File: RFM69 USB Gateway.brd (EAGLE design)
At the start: 42.3 x 17.1 mm, 22 parts, among them CN1 MINIB, IC3 MCP1703CB, U1 FT231XS, X1 16 MHz

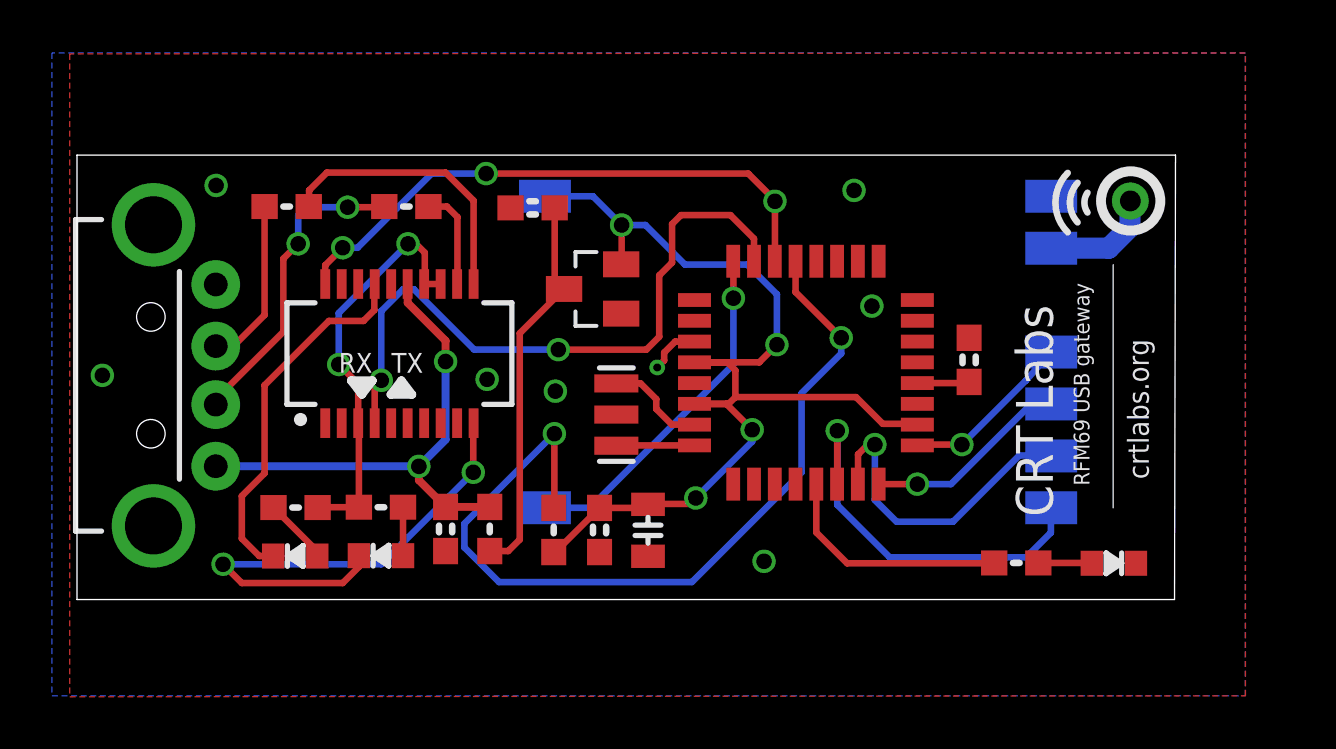
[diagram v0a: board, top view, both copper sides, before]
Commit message: Added ISP header and reset button
v0.4
- ISP header
- Reset button
- Silk screen for all components
- Slight rearrangement
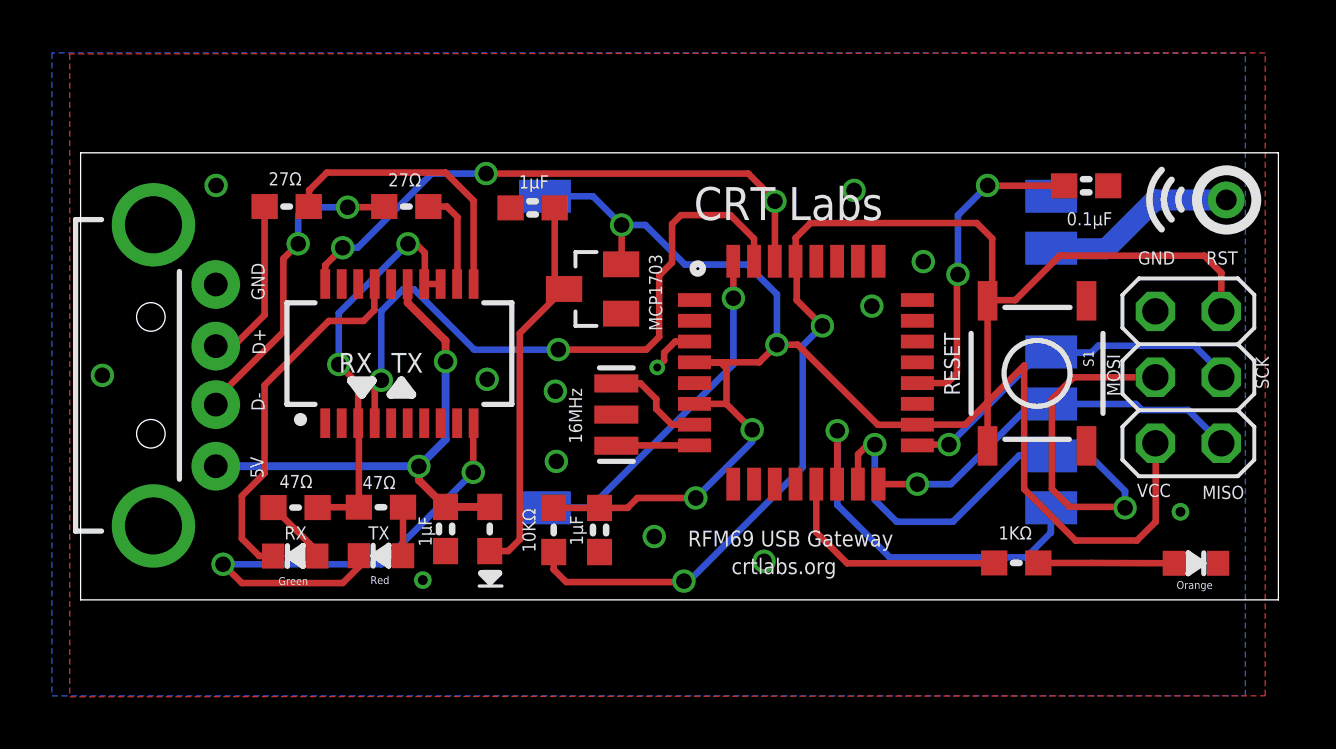
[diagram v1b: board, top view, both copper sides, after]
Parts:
- removed C3: 10u, LowPowerLab:0805-CAP
- added JP1: (no value), pinhead:2X03
- added S1: SWITCH-MOMENTARY-2SMD-ALT01, Testing:TACTILE-SWITCH-SMD-ALT01
- C4: value 0.1 -> 1u
- R2: value 1k5 -> 1k
- moved C5 8.08 mm to (50.9, 18.9), turned to 0 degrees
- moved U$1 3.70 mm to (56.3, 18.3)
- moved U$2 3.16 mm to (55.1, 4.34)
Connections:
- removed net RST: ATMEGA328.29, R1.2
- new net RESET: ATMEGA328.29, JP1.5, R1.1, S1.3, S1.4
- net D11_MOSI: now also JP1.4
- net D12_MISO: now also JP1.1
- net D13_SCK: now also JP1.3
- net GND: now also JP1.6, S1.1, S1.2; no longer C3.2
- net VCC: now also JP1.2, R1.2; no longer C3.1, R1.1
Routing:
- net RESET: track 0.00 -> 49.4 mm, vias 0 -> 2
- net RST: track 33.5 -> 0.00 mm, vias 2 -> 0
- net VCC: track 41.8 -> 57.6 mm
- net D11_MOSI: track 12.3 -> 27.3 mm, vias 1 -> 2
- net AREF: track 2.01 -> 12.4 mm, vias 0 -> 2
- net D13_SCK: track 6.68 -> 13.9 mm
- net D12_MISO: track 7.93 -> 15.1 mm
- net N$2: track 2.06 -> 5.22 mm
- net N$3: track 4.38 -> 7.53 mm
- net GND: vias 8 -> 13
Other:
- board size 42.3 x 17.1 mm -> 46.1 x 17.2 mm
- board text added: "0.1μF"
- board text added: "10KΩ"
- board text added: "16MHz"
- board text added: "1KΩ"
- board text added: "1μF"
- board text added: "27Ω"
- board text added: "47Ω"
- board text added: "5V"
- board text added: "D+"
- board text added: "D-"
- board text added: "GND"
- board text added: "Green"
- board text added: "MCP1703"
- board text added: "MISO"
- board text added: "MOSI"
- board text added: "Orange"
- board text added: "RESET"
- board text added: "RFM69 USB Gateway"
- board text added: "RST"
- board text added: "Red"
- board text added: "SCK"
- board text added: "VCC"
- board text added: "v0.4 2016"
- board text removed: "RFM69 USB gateway"
- board text removed: "v0.3 2016"

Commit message: Fixed overlapping traces
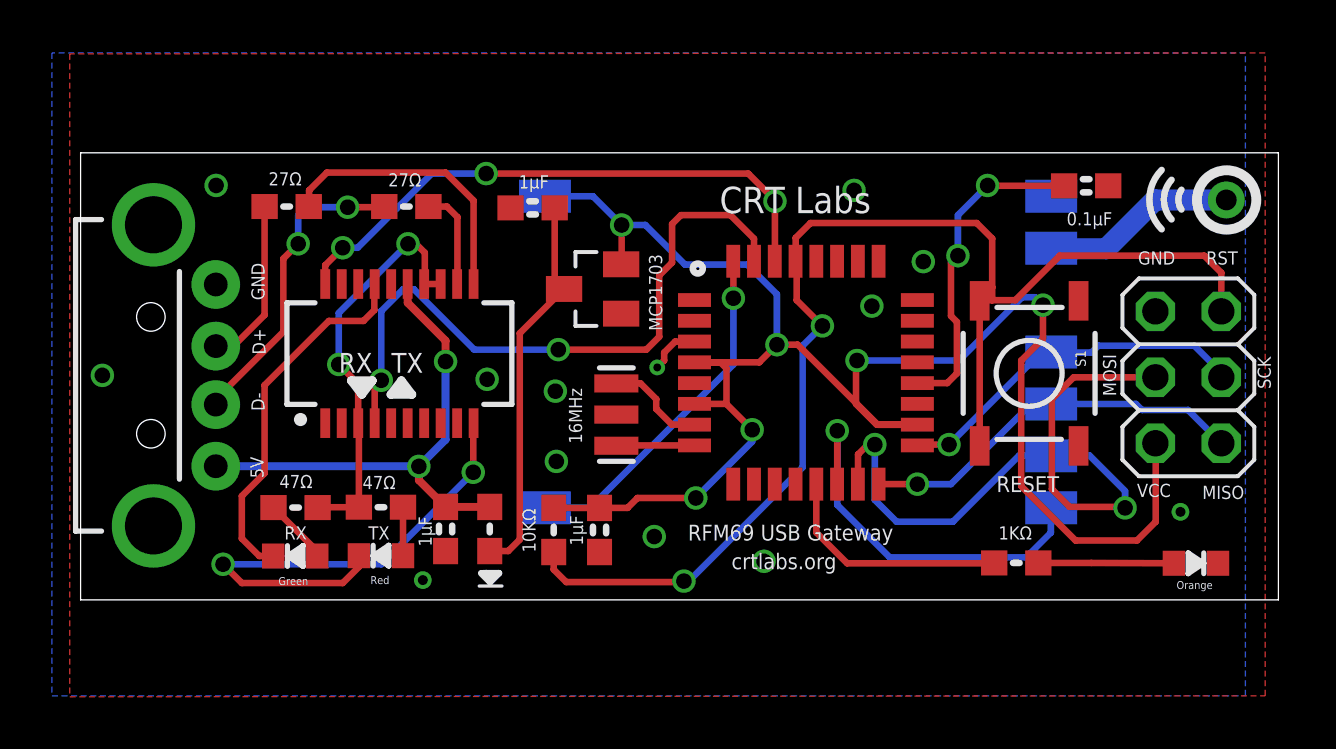
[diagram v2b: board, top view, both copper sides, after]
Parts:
- moved S1 0.30 mm to (48.7, 11.7)
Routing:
- net VCC: track 57.6 -> 68.0 mm, vias 4 -> 6
- net RESET: track 49.4 -> 49.9 mm
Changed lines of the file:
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@@
 <wire x1="27.7749" y1="3.9624" x2="27.9654" y2="3.7719" width="0.254" layer="21"/>
 <wire x1="28.3845" y1="3.4671" x2="27.5082" y2="3.4671" width="0.127" layer="21"/>
-<text x="45.4152" y="13.2207" size="0.6096" layer="121" font="vector" ratio="7" rot="R270">RESET</text>
+<text x="47.4345" y="7.0866" size="0.6096" layer="121" font="vector" ratio="7">RESET</text>
 <text x="55.5117" y="15.8496" size="0.508" layer="121" font="vector" ratio="7">RST</text>
 <text x="52.8828" y="15.8496" size="0.508" layer="121" font="vector" ratio="7">GND</text>
 <text x="52.8447" y="6.8961" size="0.508" layer="121" font="vector" ratio="7">VCC</text>
 <text x="55.3593" y="6.8199" size="0.508" layer="121" font="vector" ratio="7">MISO</text>
-<text x="52.197" y="10.7823" size="0.508" layer="121" font="vector" ratio="7" rot="R90">MOSI</text>
-<text x="57.4167" y="12.3063" size="0.508" layer="121" font="vector" ratio="7" rot="R270">SCK</text>
+<text x="52.0446" y="10.7823" size="0.508" layer="121" font="vector" ratio="7" rot="R90">MOSI</text>
+<text x="57.4929" y="12.3063" size="0.508" layer="121" font="vector" ratio="7" rot="R270">SCK</text>
 <wire x1="58.293" y1="2.9337" x2="12.1539" y2="2.9337" width="0" layer="20"/>
 <wire x1="12.1539" y1="2.9337" x2="12.1539" y2="20.1549" width="0" layer="20"/>
 <wire x1="12.1539" y1="20.1549" x2="58.293" y2="20.1549" width="0" layer="20"/>
 <wire x1="58.293" y1="20.1549" x2="58.293" y2="2.9337" width="0" layer="20"/>
-<text x="35.7759" y="17.5641" size="1.27" layer="21" font="vector" ratio="17">CRT Labs</text>
-<text x="35.5473" y="4.9911" size="0.6096" layer="21" font="vector" ratio="7">RFM69 USB Gateway</text>
-<text x="37.2237" y="3.9243" size="0.6096" layer="21" font="vector">crtlabs.org</text>
+<text x="36.7665" y="17.8308" size="1.016" layer="21" font="vector" ratio="15">CRT Labs</text>
+<text x="35.5473" y="5.2197" size="0.6096" layer="21" font="vector" ratio="7">RFM69 USB Gateway</text>
+<text x="37.2237" y="4.1148" size="0.6096" layer="21" font="vector">crtlabs.org</text>
 </plain>
 <attributes>
@@
 <attribute name="VALUE" x="59.2709" y="7.6962" size="1.27" layer="27" rot="R90"/>
 </element>
-<element name="S1" library="Testing" package="TACTILE-SWITCH-SMD-ALT01" value="SWITCH-MOMENTARY-2SMD-ALT01" x="48.9966" y="11.6586" smashed="yes" rot="R270">
-<attribute name="NAME" x="50.7746" y="12.5476" size="0.4064" layer="25" rot="R270"/>
+<element name="S1" library="Testing" package="TACTILE-SWITCH-SMD-ALT01" value="SWITCH-MOMENTARY-2SMD-ALT01" x="48.6918" y="11.6586" smashed="yes" rot="R270">
+<attribute name="NAME" x="50.4698" y="12.5476" size="0.4064" layer="25" rot="R270"/>
 </element>
 </elements>
@@
 <wire x1="44.3865" y1="11.284" x2="45.5359" y2="11.284" width="0.254" layer="1"/>
 <wire x1="45.5359" y1="11.284" x2="45.9105" y2="11.6586" width="0.254" layer="1"/>
-<wire x1="45.9105" y1="11.6586" x2="45.9105" y2="15.4305" width="0.254" layer="1"/>
-<wire x1="45.9105" y1="15.4305" x2="45.9486" y2="15.4686" width="0.254" layer="1"/>
-<via x="45.9486" y="15.4686" extent="1-16" drill="0.6" diameter="0.3048"/>
-<wire x1="45.9486" y1="15.4686" x2="45.9486" y2="17.7546" width="0.254" layer="16"/>
 <wire x1="45.9486" y1="17.7546" x2="47.0916" y2="18.8976" width="0.254" layer="16"/>
 <via x="47.0916" y="18.8976" extent="1-16" drill="0.6" diameter="0.3048"/>
 <wire x1="50.0389" y1="18.8849" x2="47.1043" y2="18.8849" width="0.254" layer="1"/>
 <wire x1="47.1043" y1="18.8849" x2="47.0916" y2="18.8976" width="0.254" layer="1"/>
+<wire x1="45.9105" y1="11.6586" x2="45.9105" y2="13.6398" width="0.254" layer="1"/>
+<wire x1="45.9105" y1="13.6398" x2="45.6819" y2="13.8684" width="0.254" layer="1"/>
+<wire x1="45.6819" y1="13.8684" x2="45.6819" y2="15.9258" width="0.254" layer="1"/>
+<wire x1="45.6819" y1="15.9258" x2="45.9486" y2="16.1925" width="0.254" layer="1"/>
+<via x="45.9486" y="16.1925" extent="1-16" drill="0.6" diameter="0.3048"/>
+<wire x1="45.9486" y1="16.1925" x2="45.9486" y2="17.7546" width="0.254" layer="16"/>
 </signal>
 <signal name="VCC">
@@
 <wire x1="30.3793" y1="6.477" x2="30.3784" y2="6.4761" width="0.254" layer="1"/>
 <contactref element="JP1" pad="2"/>
-<wire x1="44.3865" y1="9.684" x2="46.2219" y2="9.684" width="0.254" layer="1"/>
-<wire x1="46.2219" y1="9.684" x2="48.5013" y2="11.9634" width="0.254" layer="1"/>
-<wire x1="48.5013" y1="11.9634" x2="48.5013" y2="7.2009" width="0.254" layer="1"/>
-<wire x1="48.5013" y1="7.2009" x2="50.4825" y2="5.2197" width="0.254" layer="1"/>
 <wire x1="50.4825" y1="5.2197" x2="52.8447" y2="5.2197" width="0.254" layer="1"/>
 <wire x1="52.8447" y1="5.2197" x2="53.5686" y2="5.9436" width="0.254" layer="1"/>
 <wire x1="53.5686" y1="5.9436" x2="53.5686" y2="8.9535" width="0.254" layer="1"/>
 <wire x1="53.5686" y1="8.9535" x2="53.5559" y2="8.9662" width="0.254" layer="1"/>
+<wire x1="44.3865" y1="9.684" x2="42.8178" y2="9.684" width="0.254" layer="1"/>
+<wire x1="42.8178" y1="9.684" x2="42.0243" y2="10.4775" width="0.254" layer="1"/>
+<wire x1="42.0243" y1="10.4775" x2="42.0243" y2="12.1158" width="0.254" layer="1"/>
+<wire x1="42.0243" y1="12.1158" x2="42.0624" y2="12.1539" width="0.254" layer="1"/>
+<via x="42.0624" y="12.1539" extent="1-16" drill="0.6" diameter="0.3048"/>
+<wire x1="42.0624" y1="12.1539" x2="45.9867" y2="12.1539" width="0.254" layer="16"/>
+<wire x1="45.9867" y1="12.1539" x2="48.4251" y2="14.5923" width="0.254" layer="16"/>
+<wire x1="48.4251" y1="14.5923" x2="48.9204" y2="14.5923" width="0.254" layer="16"/>
+<wire x1="48.9204" y1="14.5923" x2="49.2252" y2="14.2875" width="0.254" layer="16"/>
+<via x="49.2252" y="14.2875" extent="1-16" drill="0.6" diameter="0.3048"/>
+<wire x1="49.2252" y1="14.2875" x2="49.2252" y2="12.9921" width="0.254" layer="1"/>
+<wire x1="49.2252" y1="12.9921" x2="48.387" y2="12.1539" width="0.254" layer="1"/>
+<wire x1="48.387" y1="12.1539" x2="48.387" y2="7.3152" width="0.254" layer="1"/>
+<wire x1="48.387" y1="7.3152" x2="50.4825" y2="5.2197" width="0.254" layer="1"/>
 </signal>
 <signal name="D9">
@@
 <contactref element="R1" pad="1"/>
 <contactref element="ATMEGA328" pad="29"/>
-<wire x1="47.0916" y1="14.4526" x2="47.0916" y2="8.8646" width="0.254" layer="1"/>
 <wire x1="46.6725" y1="17.4498" x2="40.2717" y2="17.4498" width="0.254" layer="1"/>
 <wire x1="40.2717" y1="17.4498" x2="39.7002" y2="16.8783" width="0.254" layer="1"/>
@@
 <wire x1="49.8729" y1="16.1925" x2="48.1584" y2="14.478" width="0.254" layer="1"/>
 <wire x1="48.1584" y1="14.478" x2="47.2694" y2="14.478" width="0.254" layer="1"/>
-<wire x1="47.2694" y1="14.478" x2="47.0916" y2="14.4526" width="0.254" layer="1"/>
-<wire x1="47.2694" y1="14.478" x2="47.2694" y2="16.8529" width="0.254" layer="1"/>
+<wire x1="47.2694" y1="14.478" x2="46.7868" y2="14.4526" width="0.254" layer="1"/>
+<wire x1="47.2694" y1="14.478" x2="47.2694" y2="14.9733" width="0.254" layer="1"/>
+<wire x1="47.2694" y1="14.9733" x2="47.2694" y2="16.8529" width="0.254" layer="1"/>
 <wire x1="47.2694" y1="16.8529" x2="46.6725" y2="17.4498" width="0.254" layer="1"/>
+<wire x1="47.0916" y1="14.7955" x2="47.2694" y2="14.9733" width="0.254" layer="1"/>
+<wire x1="46.7868" y1="8.8646" x2="46.7868" y2="14.4526" width="0.254" layer="1"/>
 </signal>
 </signals>

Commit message: Added pullup on CS (pin 10)
10K pullup on CS (RFM69) to avoid issues during ISP programming
Changed all components to 0805 size
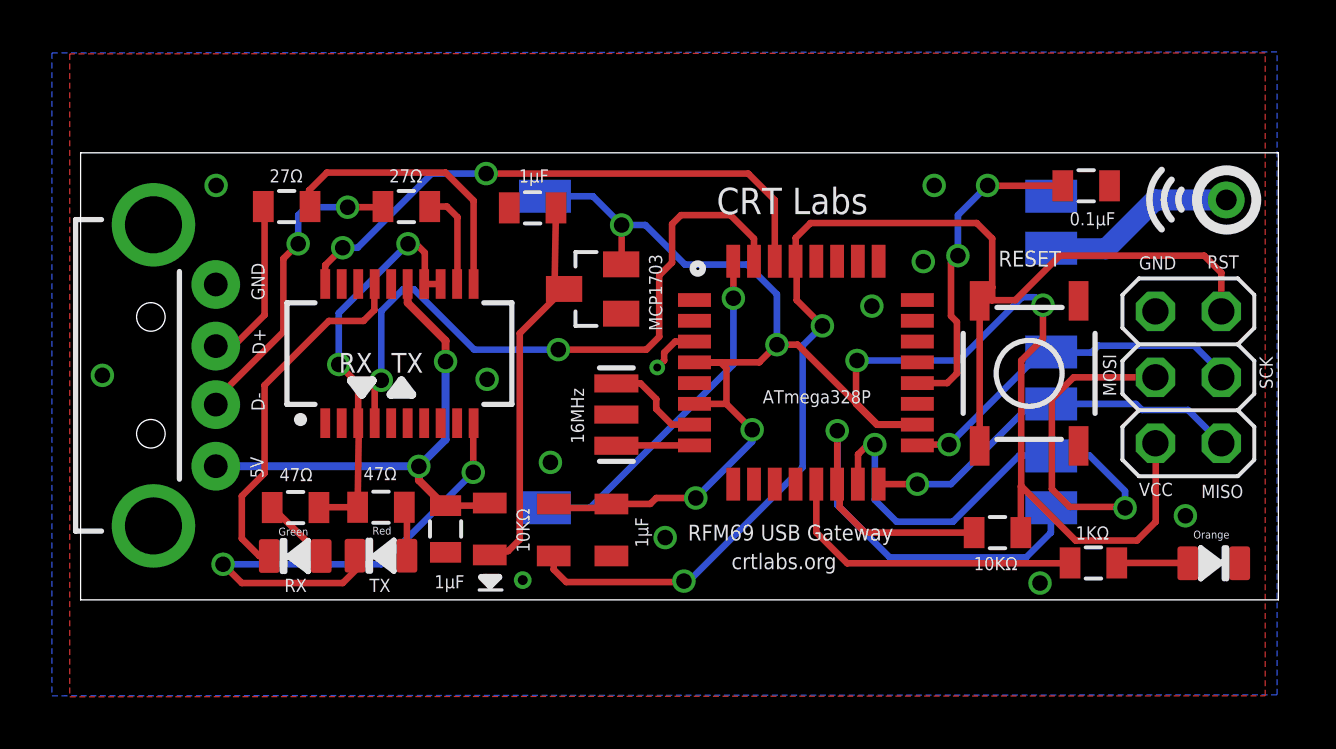
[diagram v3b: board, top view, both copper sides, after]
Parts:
- added R7: 10K, SparkFun:0805
- C2, C5, C6: device LowPowerLab:0603-CAP -> SparkFun:0805
- C4: device LowPowerLab:0603-CAP -> LowPowerLab:0805
- D, R1: device LowPowerLab:0603-RES -> LowPowerLab:0805
- R2, R3, R4, R5, R6: device LowPowerLab:0603-RES -> SparkFun:0805
- U$2, U$4, U$7: value LED0603 -> LED0805; device LowPowerLab:0603-LED -> LowPowerLab:0805-LED
- moved R2 2.97 mm to (51.2, 4.36)
- moved U$2 0.69 mm to (55.8, 4.34)
- moved C4 0.46 mm to (32.6, 5.63)
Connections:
- net D10_SS: now also R7.1
- net VCC: now also R7.2
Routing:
- net D10_SS: track 15.3 -> 21.9 mm
- net D9: track 9.21 -> 12.2 mm
- net N$2: track 5.22 -> 2.74 mm
- net VCC: track 68.0 -> 70.4 mm
- net D0_RX: vias 3 -> 2
- net GND: vias 13 -> 12
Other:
- board text added: "ANT"
- board text added: "ATmega328P"
- board text added: "v0.5 2016"
- board text removed: "v0.4 2016"

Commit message: v0.6 - fixed auto reset, adjusted traces
Added 0.1 uF cap on reset, series with DTR (allows auto reset via FTDI)
Moved some components to accommodate the cap
Adjusted several traces
Made GND vias more consistent in size
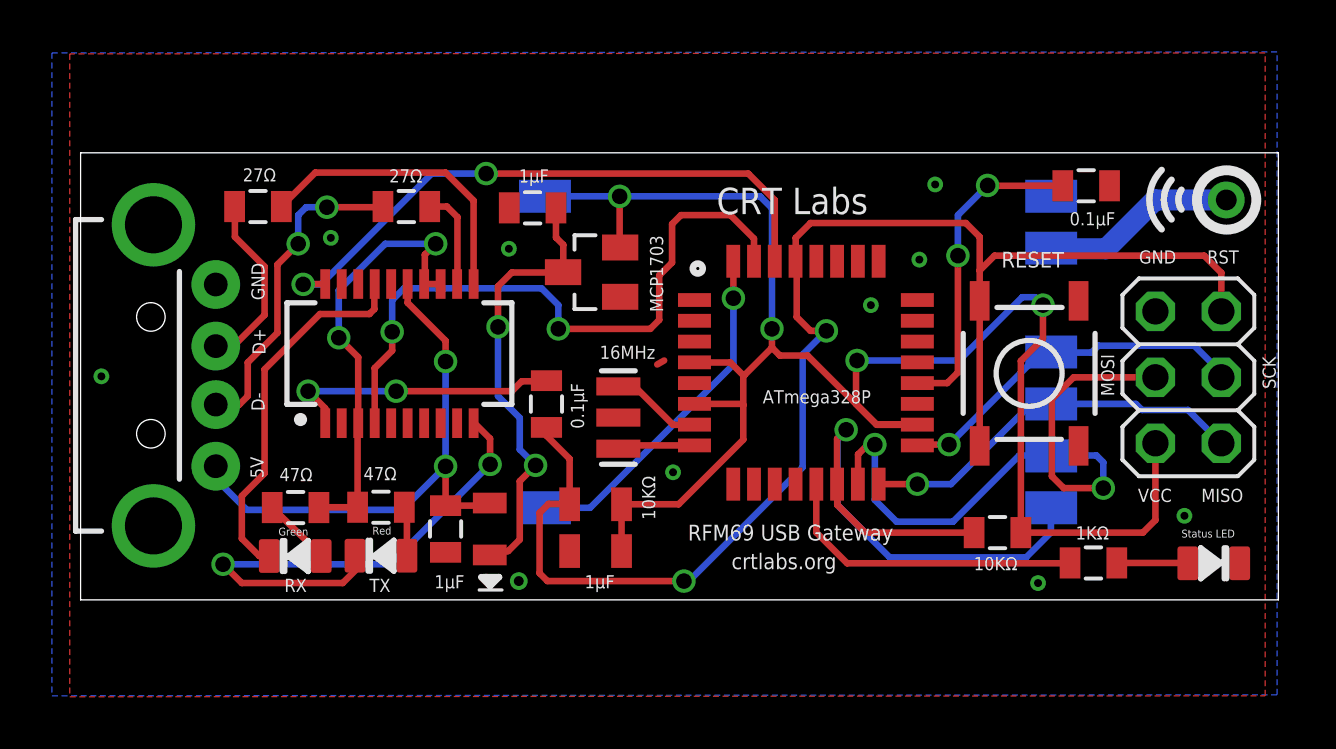
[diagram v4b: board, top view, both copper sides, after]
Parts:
- added C1: 0.1, SparkFun:0805
- moved R1 1.89 mm to (32.0, 6.62), turned to 0 degrees
- moved R5 1.10 mm to (19.0, 18.1)
- moved C4 1.02 mm to (32.0, 4.81), turned to 180 degrees
- moved IC3 0.65 mm to (31.8, 15.6)
- moved X1 0.14 mm to (32.9, 9.96)
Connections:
- net DTR: now also C1.1
- net RESET: now also C1.2
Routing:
- net DTR: track 0.00 -> 10.9 mm, vias 0 -> 2
- net RESET: track 49.8 -> 56.0 mm
- net D11_MOSI: track 27.3 -> 24.9 mm
- net VIN: track 15.0 -> 17.3 mm, vias 0 -> 2
- net VBUS: track 19.7 -> 21.5 mm
- net GND: track 2.03 -> 0.31 mm, vias 12 -> 10
- net VCC: track 70.4 -> 68.8 mm, vias 6 -> 4
- net FTDI3.3V: track 15.8 -> 17.1 mm
- net D0_RX: track 22.3 -> 23.6 mm
- net N$7: track 19.3 -> 20.0 mm
- net N$5: track 10.9 -> 11.6 mm
- net D-: track 12.0 -> 12.5 mm
- net D10_SS: track 21.9 -> 22.4 mm
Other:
- board text added: "Status LED"
- board text added: "v0.6 2016"
- board text removed: "Orange"
- board text removed: "v0.5 2016"
